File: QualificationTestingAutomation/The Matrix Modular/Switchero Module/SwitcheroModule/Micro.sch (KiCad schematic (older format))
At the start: 10 parts, among them SW1 SW_DIP_x04, U1 TC2050-JTAG-SchematicAutomati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, U2 AT25SF081-SSHD-X, U3 MSP430G2755IRHA40, U4 SN74HC266DR, U5 SN74LVC08APWR

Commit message: Cleaned up the libraries Cleaned up the tracks Adjusted footprints to the manufacturers minimum size.
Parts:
- R1, R2, R3, R4: symbol TheMatrix-rescue:RESISTOR-passive-SchematicAutomation-rescue -> SwitcheroModule-rescue:RESISTOR-passive-SchematicAutomation-rescue-TheMatrix-rescue
- U1: symbol TheMatrix-rescue:TC2050-JTAG-SchematicAutomation-rescue -> SwitcheroModule-rescue:TC2050-JTAG-SchematicAutomation-rescue-TheMatrix-rescue
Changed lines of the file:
@@
 $EndComp
 $Comp
-L TheMatrix-rescue:TC2050-JTAG-SchematicAutomation-rescue U1
+L SwitcheroModule-rescue:TC2050-JTAG-SchematicAutomation-rescue-TheMatrix-rescue U1
 U 1 1 5CB44B9C
 P 1850 4100
@@
 S3
 $Comp
-L TheMatrix-rescue:RESISTOR-passive-SchematicAutomation-rescue R?
+L SwitcheroModule-rescue:RESISTOR-passive-SchematicAutomation-rescue-TheMatrix-rescue R?
 U 1 1 5CB45035
 P 7000 2850
@@
 $EndComp
 $Comp
-L TheMatrix-rescue:RESISTOR-passive-SchematicAutomation-rescue R?
+L SwitcheroModule-rescue:RESISTOR-passive-SchematicAutomation-rescue-TheMatrix-rescue R?
 U 1 1 5CB450E2
 P 6850 2700
@@
 $EndComp
 $Comp
-L TheMatrix-rescue:RESISTOR-passive-SchematicAutomation-rescue R?
+L SwitcheroModule-rescue:RESISTOR-passive-SchematicAutomation-rescue-TheMatrix-rescue R?
 U 1 1 5CB450FF
 P 6750 2600
@@
 $EndComp
 $Comp
-L TheMatrix-rescue:RESISTOR-passive-SchematicAutomation-rescue R?
+L SwitcheroModule-rescue:RESISTOR-passive-SchematicAutomation-rescue-TheMatrix-rescue R?
 U 1 1 5CB45139
 P 6600 2500

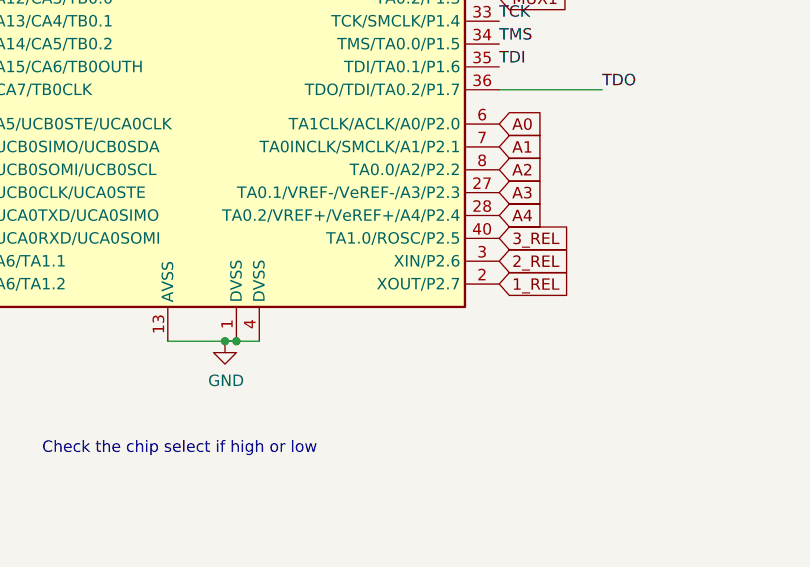
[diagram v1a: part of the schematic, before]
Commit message: Added Voltage and current measurment of the muxes and relays to the MSP Some clean up of the tracks.
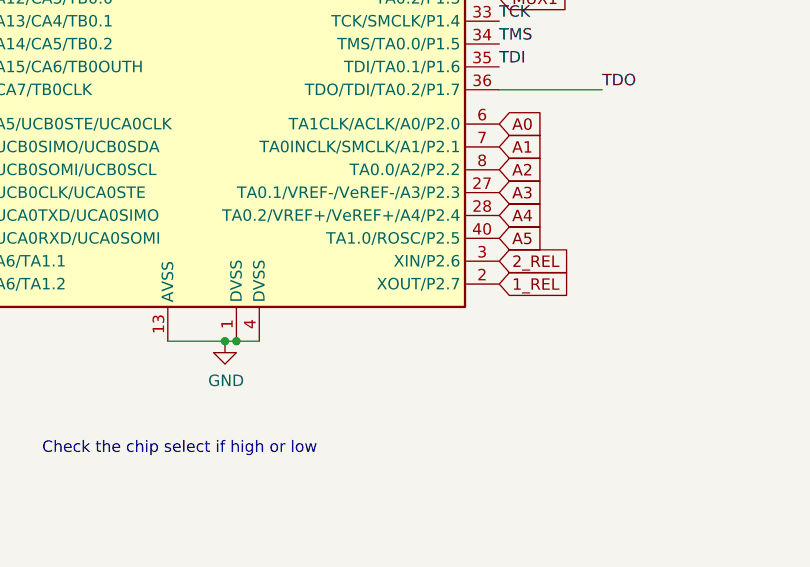
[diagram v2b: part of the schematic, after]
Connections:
- net 3_REL renamed A5
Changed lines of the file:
@@
 EESchema Schematic File Version 4
 LIBS:SwitcheroModule-cache
-EELAYER 26 0
+EELAYER 29 0
 EELAYER END
 $Descr A4 11693 8268
@@
 Text GLabel 6250 4950 2    50   Input ~ 0
 2_REL
-Text GLabel 6250 4850 2    50   Input ~ 0
-3_REL
 $Comp
 L power:+3V3 #PWR0105
@@
 Text Notes 4250 5800 0    50   ~ 0
 Check the chip select if high or low
-Wire Wire Line
-	5100 5300 5050 5300
 Connection ~ 5050 5300
 Wire Wire Line
 	5050 5300 4800 5300
+Text GLabel 6250 4850 2    50   Input ~ 0
+A5
 $EndSCHEMATC

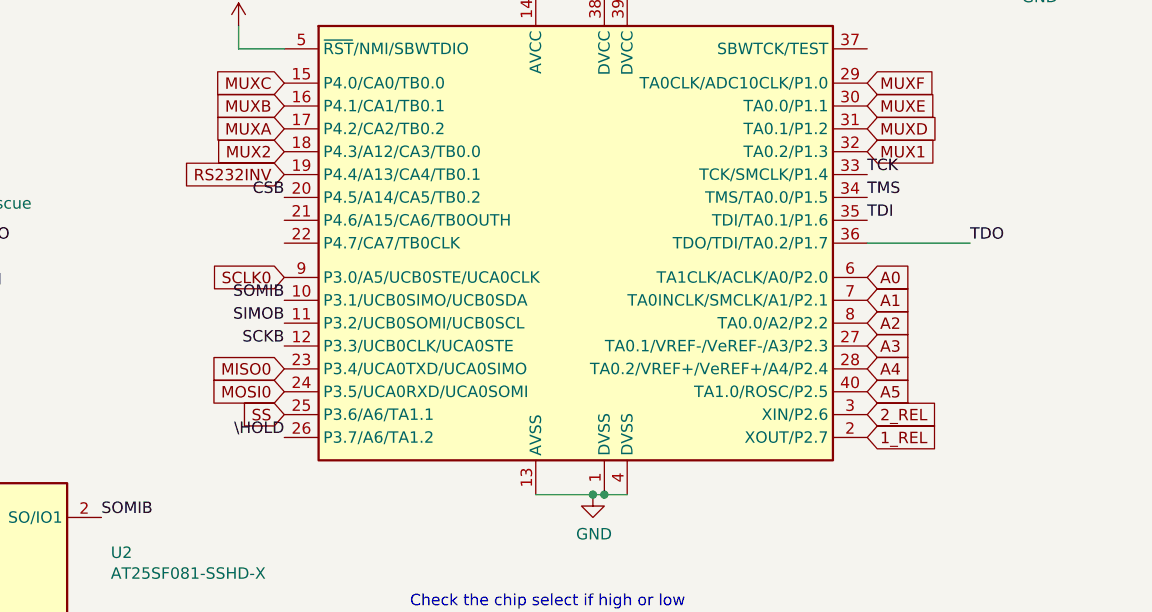
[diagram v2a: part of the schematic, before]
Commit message: Updated the layout to accomodate the voltage and current sensing.
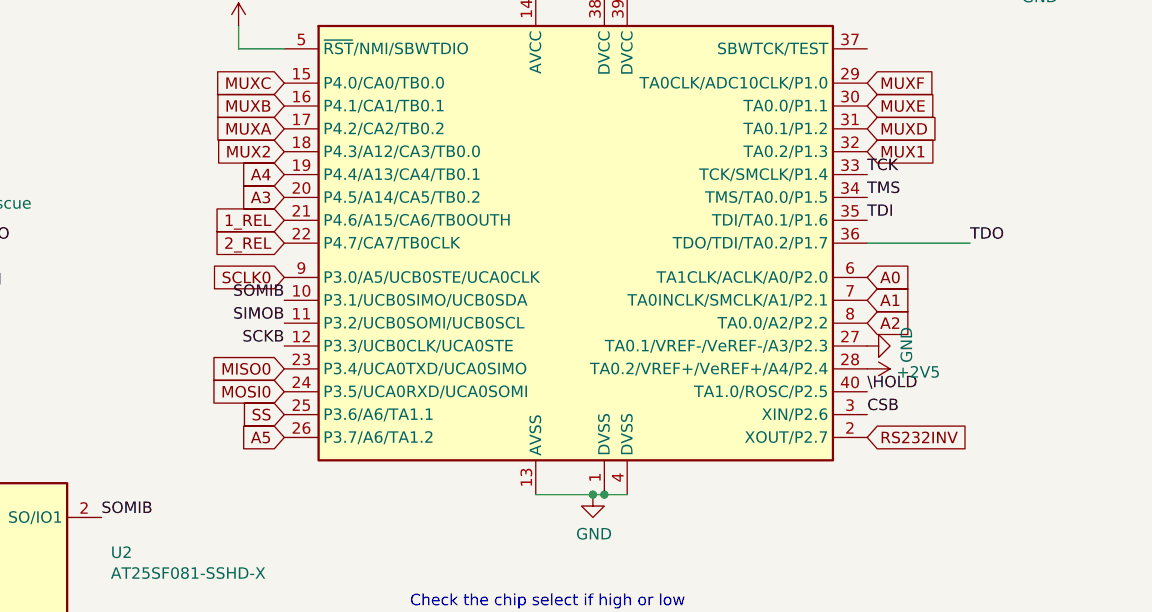
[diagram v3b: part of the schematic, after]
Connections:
- net 1_REL: now also U3.21 (P4.6/A15/CA6/TB0OUTH); no longer U3.2 (XOUT/P2.7)
- net 2_REL: now also U3.22 (P4.7/CA7/TB0CLK); no longer U3.3 (XIN/P2.6)
- net A3: now also U3.20 (P4.5/A14/CA5/TB0.2); no longer U3.27 (TA0.1/VREF-/VeREF-/A3/P2.3)
- net A4: now also U3.19 (P4.4/A13/CA4/TB0.1); no longer U3.28 (TA0.2/VREF+/VeREF+/A4/P2.4)
- net A5: now also U3.26 (P3.7/A6/TA1.2); no longer U3.40 (TA1.0/ROSC/P2.5)
- net CSB: now also U3.3 (XIN/P2.6); no longer U3.20 (P4.5/A14/CA5/TB0.2)
- net GND: now also U3.27 (TA0.1/VREF-/VeREF-/A3/P2.3)
- net RS232INV: now also U3.2 (XOUT/P2.7); no longer U3.19 (P4.4/A13/CA4/TB0.1)
- net \HOLD: now also U3.40 (TA1.0/ROSC/P2.5); no longer U3.26 (P3.7/A6/TA1.2)
- new net +2V5: U3.28 (TA0.2/VREF+/VeREF+/A4/P2.4)
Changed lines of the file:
@@
 Text GLabel 6250 3800 2    50   Input ~ 0
 MUX1
-Text GLabel 6250 5050 2    50   Input ~ 0
+Text GLabel 3700 4100 0    50   Input ~ 0
 1_REL
-Text GLabel 6250 4950 2    50   Input ~ 0
+Text GLabel 3700 4200 0    50   Input ~ 0
 2_REL
 $Comp
@@
 Text GLabel 6250 4550 2    50   Input ~ 0
 A2
-Text GLabel 6250 4650 2    50   Input ~ 0
-A3
-Text GLabel 6250 4750 2    50   Input ~ 0
-A4
-Text Label 3700 5050 2    50   ~ 0
+Text Label 6250 4850 0    50   ~ 0
 \HOLD
 Wire Wire Line
@@
 Wire Wire Line
 	10500 2700 10650 2700
-Text GLabel 3700 3900 0    50   Input ~ 0
+Text GLabel 6250 5050 2    50   Input ~ 0
 RS232INV
 Wire Wire Line
@@
 Wire Wire Line
 	6600 2950 6600 2600
-Text Label 3700 4000 2    50   ~ 0
+Text Label 6250 4950 0    50   ~ 0
 CSB
 Text GLabel 3700 4950 0    50   Input ~ 0
@@
 Wire Wire Line
 	5050 5300 4800 5300
-Text GLabel 6250 4850 2    50   Input ~ 0
+Text GLabel 3700 5050 0    50   Input ~ 0
 A5
+$Comp
+L power:+2V5 #PWR?
+U 1 1 5CA7FFF6
+P 6250 4750
+F 0 "#PWR?" H 6250 4600 50  0001 C CNN
+F 1 "+2V5" V 6265 4878 50  0000 L CNN
+F 2 "" H 6250 4750 50  0001 C CNN
+F 3 "" H 6250 4750 50  0001 C CNN
+	1    6250 4750
+	0    1    1    0
+$EndComp
+$Comp
+L power:GND #PWR?
+U 1 1 5CA8286A
+P 6250 4650
+F 0 "#PWR?" H 6250 4400 50  0001 C CNN
+F 1 "GND" H 6255 4477 50  0000 C CNN
+F 2 "" H 6250 4650 50  0001 C CNN
+F 3 "" H 6250 4650 50  0001 C CNN
+	1    6250 4650
+	0    -1   -1   0
+$EndComp
+Text GLabel 3700 3900 0    50   Input ~ 0
+A4
+Text GLabel 3700 4000 0    50   Input ~ 0
+A3
 $EndSCHEMATC

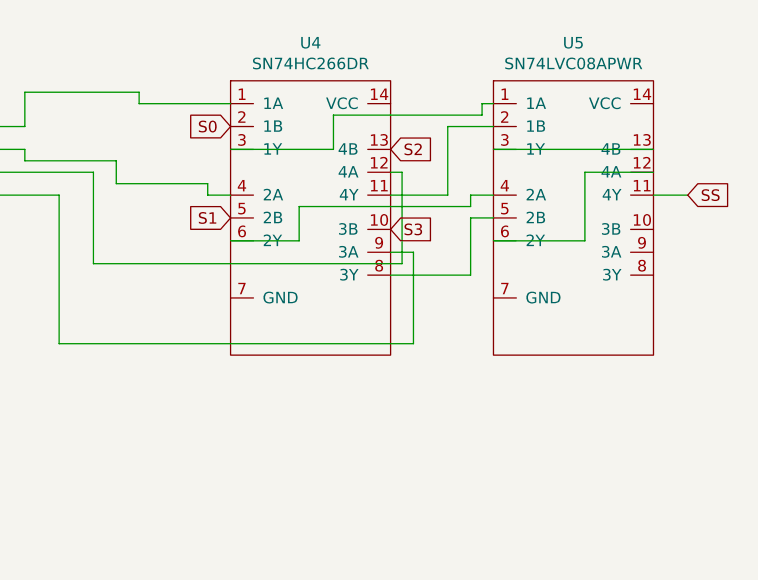
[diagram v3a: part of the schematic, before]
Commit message: Schematic Clean ups the layout needs to be changed
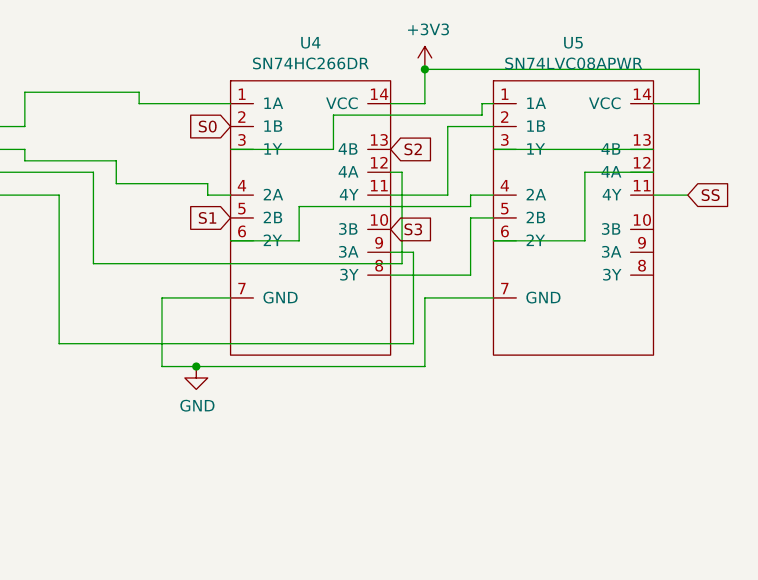
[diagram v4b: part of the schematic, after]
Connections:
- net +3V3: now also U4.14 (VCC), U5.14 (VCC)
- net GND: now also U4.7 (GND), U5.7 (GND)
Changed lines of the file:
@@
 A5
 $Comp
-L power:+2V5 #PWR?
+L power:+2V5 #PWR0182
 U 1 1 5CA7FFF6
 P 6250 4750
-F 0 "#PWR?" H 6250 4600 50  0001 C CNN
+F 0 "#PWR0182" H 6250 4600 50  0001 C CNN
 F 1 "+2V5" V 6265 4878 50  0000 L CNN
 F 2 "" H 6250 4750 50  0001 C CNN
@@
 $EndComp
 $Comp
-L power:GND #PWR?
+L power:GND #PWR0216
 U 1 1 5CA8286A
 P 6250 4650
-F 0 "#PWR?" H 6250 4400 50  0001 C CNN
+F 0 "#PWR0216" H 6250 4400 50  0001 C CNN
 F 1 "GND" H 6255 4477 50  0000 C CNN
 F 2 "" H 6250 4650 50  0001 C CNN
@@
 Text GLabel 3700 4000 0    50   Input ~ 0
 A3
+$Comp
+L power:+3V3 #PWR0230
+U 1 1 5CB308E4
+P 9500 2150
+F 0 "#PWR0230" H 9500 2000 50  0001 C CNN
+F 1 "+3V3" H 9515 2323 50  0000 C CNN
+F 2 "" H 9500 2150 50  0001 C CNN
+F 3 "" H 9500 2150 50  0001 C CNN
+	1    9500 2150
+	1    0    0    -1
+$EndComp
+Wire Wire Line
+	9500 2150 9500 2300
+Wire Wire Line
+	9500 2300 9350 2300
+Connection ~ 9500 2150
+Wire Wire Line
+	10700 2150 10700 2300
+Wire Wire Line
+	10700 2300 10500 2300
+Wire Wire Line
+	9500 2150 10700 2150
+Wire Wire Line
+	9800 3150 9500 3150
+Wire Wire Line
+	9500 3150 9500 3450
+Wire Wire Line
+	9500 3450 8500 3450
+Wire Wire Line
+	8350 3450 8350 3150
+Wire Wire Line
+	8350 3150 8650 3150
+$Comp
+L power:GND #PWR0231
+U 1 1 5CB3B256
+P 8500 3450
+F 0 "#PWR0231" H 8500 3200 50  0001 C CNN
+F 1 "GND" H 8505 3277 50  0000 C CNN
+F 2 "" H 8500 3450 50  0001 C CNN
+F 3 "" H 8500 3450 50  0001 C CNN
+	1    8500 3450
+	1    0    0    -1
+$EndComp
+Connection ~ 8500 3450
+Wire Wire Line
+	8500 3450 8350 3450
 $EndSCHEMATC

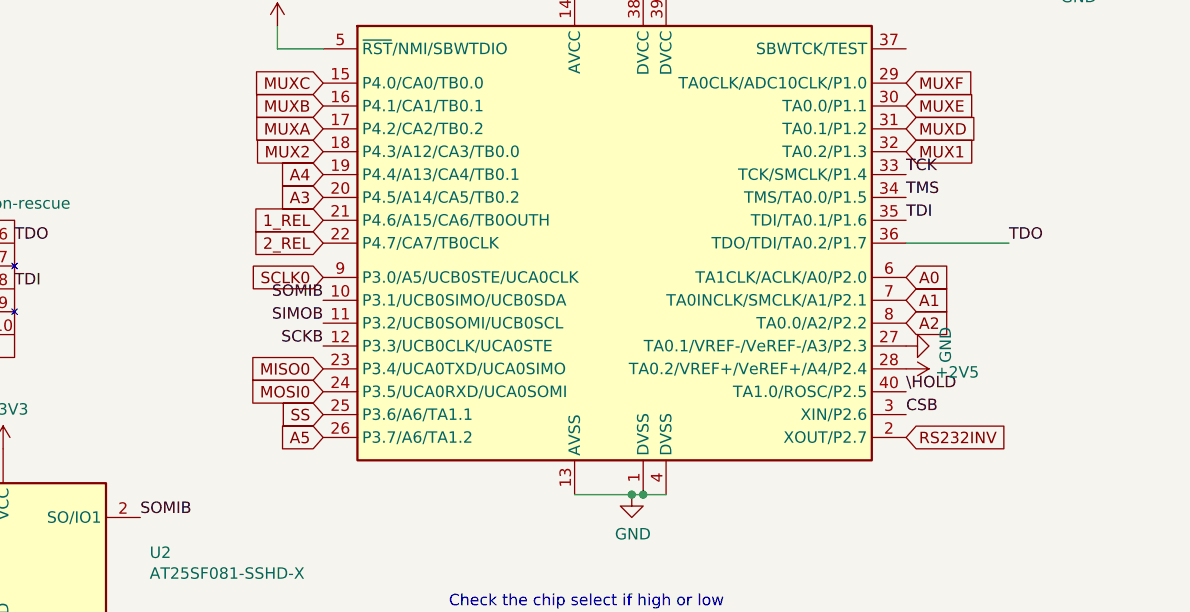
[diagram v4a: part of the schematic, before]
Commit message: IO clean up added the 1v25 reference to Matrix Changed Some of the labels to more legible names.
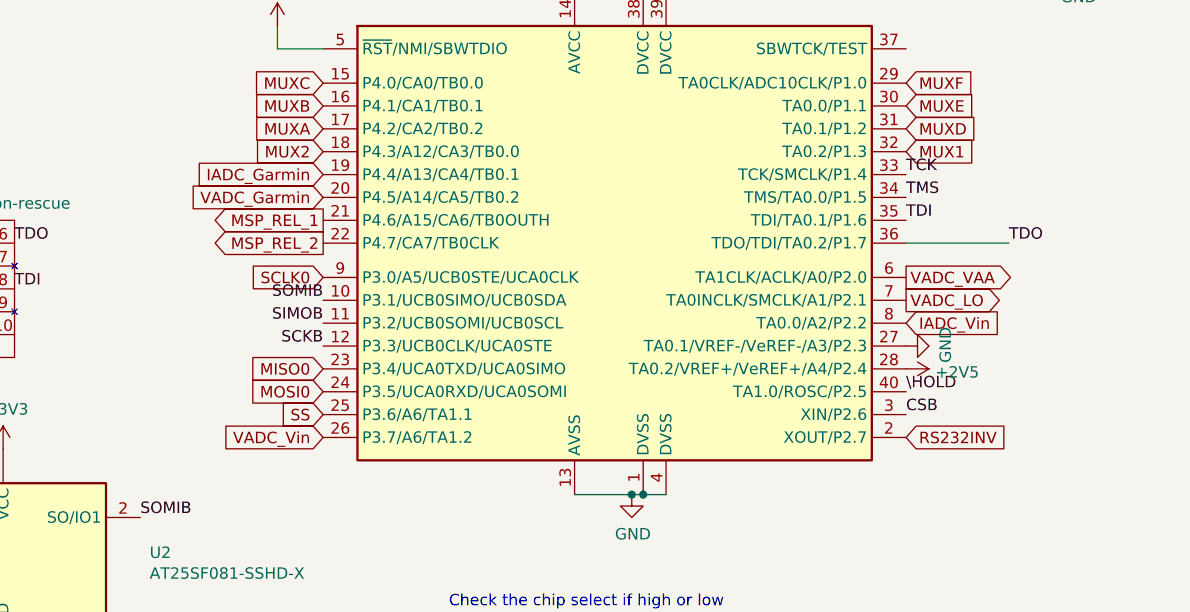
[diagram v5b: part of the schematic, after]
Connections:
- net 1_REL renamed MSP_REL_1
- net 2_REL renamed MSP_REL_2
- net A0 renamed VADC_VAA
- net A1 renamed VADC_LO
- net A2 renamed IADC_Vin
- net A3 renamed VADC_Garmin
- net A4 renamed IADC_Garmin
- net A5 renamed VADC_Vin
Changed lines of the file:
@@
 Text GLabel 6250 3800 2    50   Input ~ 0
 MUX1
-Text GLabel 3700 4100 0    50   Input ~ 0
-1_REL
-Text GLabel 3700 4200 0    50   Input ~ 0
-2_REL
 $Comp
 L power:+3V3 #PWR0105
@@
 Text Label 3700 4650 2    50   ~ 0
 SCKB
-Text GLabel 6250 4350 2    50   Input ~ 0
-A0
-Text GLabel 6250 4450 2    50   Input ~ 0
-A1
-Text GLabel 6250 4550 2    50   Input ~ 0
-A2
 Text Label 6250 4850 0    50   ~ 0
 \HOLD
@@
 Wire Wire Line
 	5050 5300 4800 5300
-Text GLabel 3700 5050 0    50   Input ~ 0
-A5
 $Comp
 L power:+2V5 #PWR0182
@@
 	0    -1   -1   0
 $EndComp
-Text GLabel 3700 3900 0    50   Input ~ 0
-A4
-Text GLabel 3700 4000 0    50   Input ~ 0
-A3
 $Comp
 L power:+3V3 #PWR0230
@@
 Wire Wire Line
 	8500 3450 8350 3450
+Text GLabel 6250 4550 2    50   Input ~ 0
+IADC_Vin
+Text GLabel 3700 5050 0    50   Input ~ 0
+VADC_Vin
+Text GLabel 3700 4000 0    50   Input ~ 0
+VADC_Garmin
+Text GLabel 3700 3900 0    50   Input ~ 0
+IADC_Garmin
+Text GLabel 3700 4100 0    50   Output ~ 0
+MSP_REL_1
+Text GLabel 3700 4200 0    50   Output ~ 0
+MSP_REL_2
+Text GLabel 6250 4350 2    50   Output ~ 0
+VADC_VAA
+Text GLabel 6250 4450 2    50   Output ~ 0
+VADC_LO
 $EndSCHEMATC

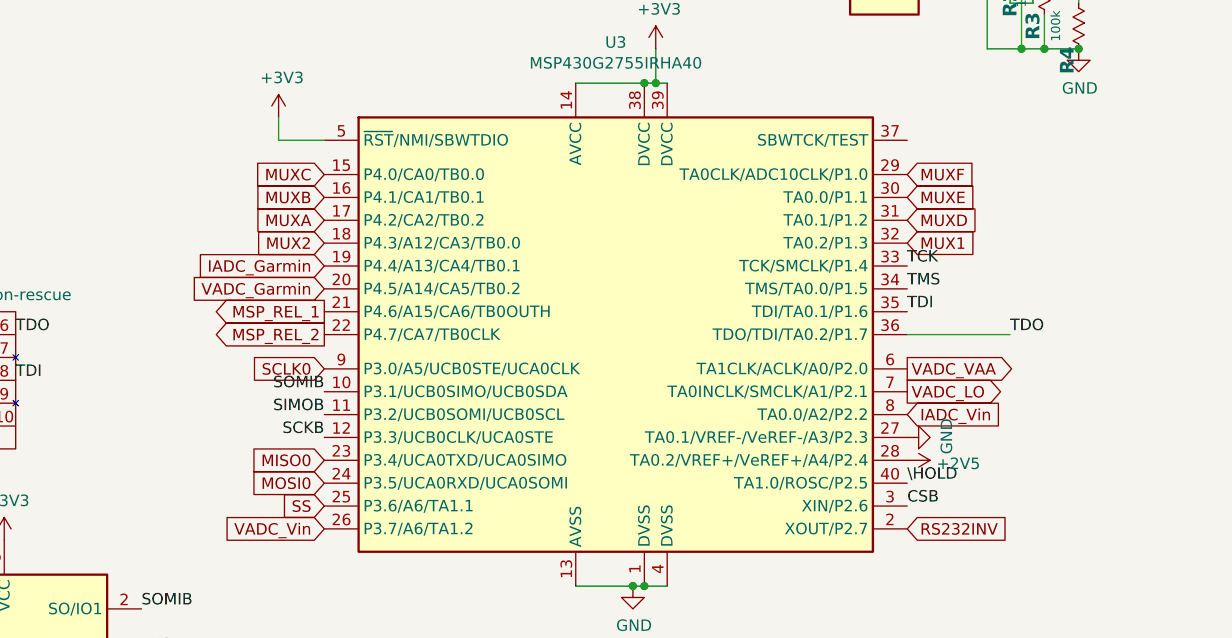
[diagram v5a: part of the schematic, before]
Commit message: Reefero Module PCB design
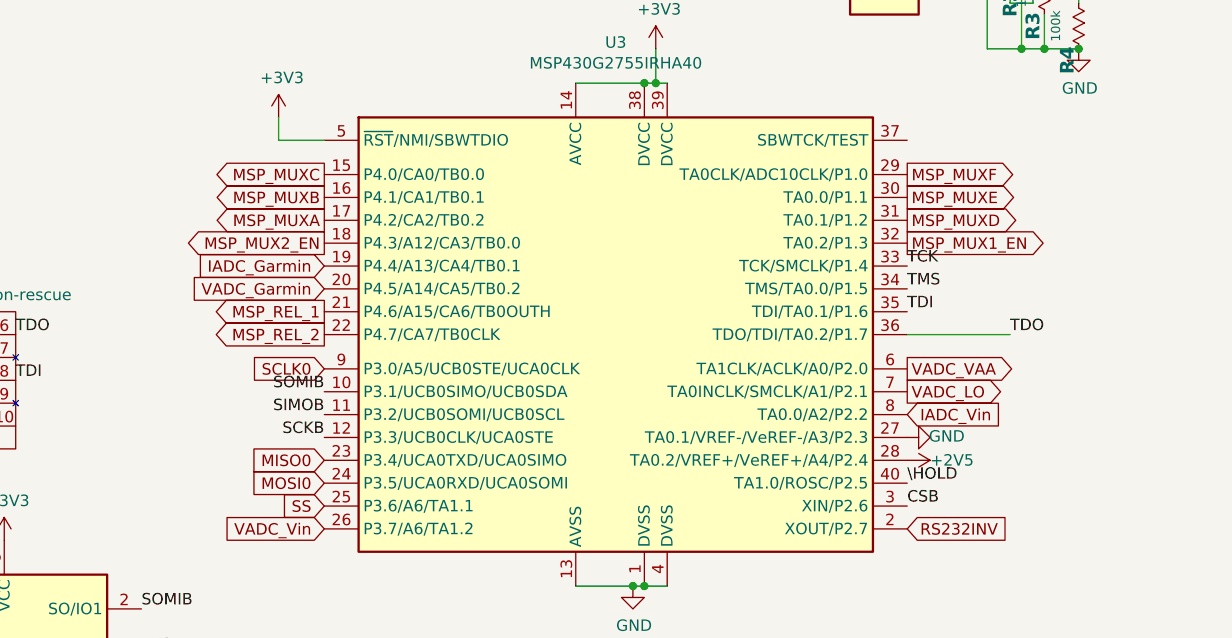
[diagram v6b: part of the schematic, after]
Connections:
- net MUX1 renamed MSP_MUX1_EN
- net MUX2 renamed MSP_MUX2_EN
- net MUXA renamed MSP_MUXA
- net MUXB renamed MSP_MUXB
- net MUXC renamed MSP_MUXC
- net MUXD renamed MSP_MUXD
- net MUXE renamed MSP_MUXE
- net MUXF renamed MSP_MUXF
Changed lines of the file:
@@
 Wire Wire Line
 	7000 2700 7900 2700
-Text GLabel 3700 3700 0    50   Input ~ 0
-MUXA
-Text GLabel 3700 3600 0    50   Input ~ 0
-MUXB
-Text GLabel 3700 3500 0    50   Input ~ 0
-MUXC
-Text GLabel 3700 3800 0    50   Input ~ 0
-MUX2
-Text GLabel 6250 3500 2    50   Input ~ 0
-MUXF
-Text GLabel 6250 3700 2    50   Input ~ 0
-MUXD
-Text GLabel 6250 3600 2    50   Input ~ 0
-MUXE
-Text GLabel 6250 3800 2    50   Input ~ 0
-MUX1
+Text GLabel 3700 3700 0    50   Output ~ 0
+MSP_MUXA
+Text GLabel 3700 3600 0    50   Output ~ 0
+MSP_MUXB
+Text GLabel 3700 3500 0    50   Output ~ 0
+MSP_MUXC
+Text GLabel 6250 3500 2    50   Output ~ 0
+MSP_MUXF
+Text GLabel 6250 3700 2    50   Output ~ 0
+MSP_MUXD
+Text GLabel 6250 3600 2    50   Output ~ 0
+MSP_MUXE
 $Comp
 L power:+3V3 #PWR0105
@@
 P 6250 4750
 F 0 "#PWR0182" H 6250 4600 50  0001 C CNN
-F 1 "+2V5" V 6265 4878 50  0000 L CNN
+F 1 "+2V5" V 6250 4850 50  0000 L CNN
 F 2 "" H 6250 4750 50  0001 C CNN
 F 3 "" H 6250 4750 50  0001 C CNN
@@
 P 6250 4650
 F 0 "#PWR0216" H 6250 4400 50  0001 C CNN
-F 1 "GND" H 6255 4477 50  0000 C CNN
+F 1 "GND" V 6255 4477 50  0000 C CNN
 F 2 "" H 6250 4650 50  0001 C CNN
 F 3 "" H 6250 4650 50  0001 C CNN
@@
 Text GLabel 6250 4450 2    50   Output ~ 0
 VADC_LO
+Text GLabel 6250 3800 2    50   Output ~ 0
+MSP_MUX1_EN
+Text GLabel 3700 3800 0    50   Output ~ 0
+MSP_MUX2_EN
 $EndSCHEMATC
